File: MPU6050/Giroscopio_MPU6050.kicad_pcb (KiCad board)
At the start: 2 copper layers, 15.1 x 16.7 mm, 7 parts, among them U301 MPU-6050

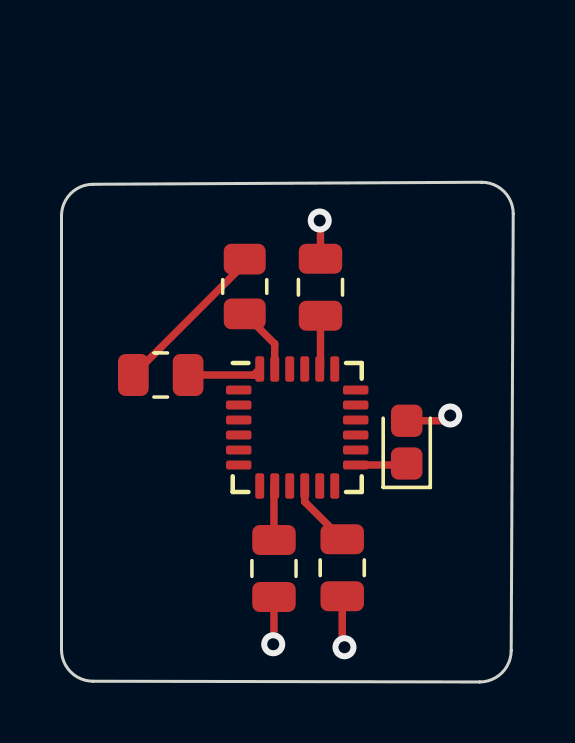
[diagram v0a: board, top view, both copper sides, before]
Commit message: MPU6050: modificato il leggermente il disegno
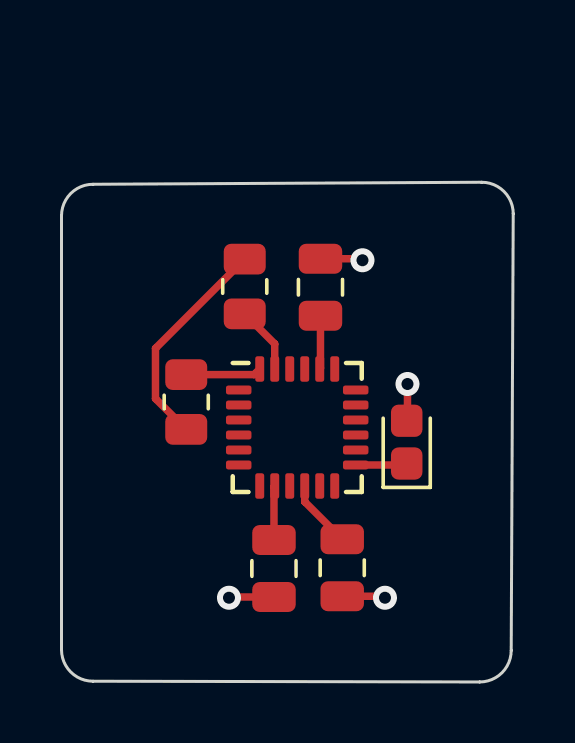
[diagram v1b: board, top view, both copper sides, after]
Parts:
- moved R401 1.24 mm to (158.8, 63.2), turned to 90 degrees
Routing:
- net VCC_3.3v: track 5.40 -> 7.48 mm
- net GND: track 6.12 -> 5.61 mm
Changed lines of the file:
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@@
   )
   (footprint "Resistor_SMD:R_0805_2012Metric" (layer "F.Cu")
-    (at 157.95 62.3)
+    (at 158.8 63.2 90)
     (descr "Resistor SMD 0805 (2012 Metric), square (rectangular) end terminal, IPC_7351 nominal, (Body size source: IPC-SM-782 page 72, https://www.pcb-3d.com/wordpress/wp-content/uploads/ipc-sm-782a_amendment_1_and_2.pdf), generated with kicad-footprint-generator")
     (tags "resistor")
@@
     (property "Sheetname" "")
     (attr smd)
-    (fp_text reference "R401" (at 0 -1.65) (layer "F.Fab")
+    (fp_text reference "R401" (at 0 -1.65 90) (layer "F.Fab")
       (effects (font (size 1 1) (thickness 0.15)))
     )
-    (fp_text value "4.7k" (at 0 1.65) (layer "F.Fab")
+    (fp_text value "4.7k" (at 0 1.65 90) (layer "F.Fab")
       (effects (font (size 1 1) (thickness 0.15)))
     )
-    (fp_text user "${REFERENCE}" (at 0 0) (layer "F.Fab")
+    (fp_text user "${REFERENCE}" (at 0 0 90) (layer "F.Fab")
       (effects (font (size 0.5 0.5) (thickness 0.08)))
     )
@@
     (fp_line (start -1 0.625) (end -1 -0.625) (layer "F.Fab") (width 0.1))
     (fp_line (start 1 -0.625) (end 1 0.625) (layer "F.Fab") (width 0.1))
-    (pad "1" smd roundrect (at -0.9125 0) (size 1.025 1.4) (layers "F.Cu" "F.Paste" "F.Mask") (roundrect_rratio 0.243902)
+    (pad "1" smd roundrect (at -0.9125 0 90) (size 1.025 1.4) (layers "F.Cu" "F.Paste" "F.Mask") (roundrect_rratio 0.243902)
       (net 6 "VCC_3.3v") (pintype "passive"))
-    (pad "2" smd roundrect (at 0.9125 0) (size 1.025 1.4) (layers "F.Cu" "F.Paste" "F.Mask") (roundrect_rratio 0.243902)
+    (pad "2" smd roundrect (at 0.9125 0 90) (size 1.025 1.4) (layers "F.Cu" "F.Paste" "F.Mask") (roundrect_rratio 0.243902)
       (net 7 "Net-(U301-Pad24)") (pintype "passive"))
     (model "${KICAD6_3DMODEL_DIR}/Resistor_SMD.3dshapes/R_0805_2012Metric.wrl"
@@
   (segment (start 166.15 65.25) (end 166.1 65.3) (width 0.25) (layer "F.Cu") (net 1))
   (segment (start 166.1 65.3) (end 164.45 65.3) (width 0.25) (layer "F.Cu") (net 1))
-  (segment (start 166.15 63.825) (end 167.425 63.825) (width 0.25) (layer "F.Cu") (net 2))
-  (segment (start 161.725 71.25) (end 161.7 71.275) (width 0.25) (layer "F.Cu") (net 2))
-  (segment (start 164 71.3) (end 164.075 71.375) (width 0.25) (layer "F.Cu") (net 2))
-  (segment (start 163.275 57.175) (end 163.25 57.15) (width 0.25) (layer "F.Cu") (net 2))
-  (segment (start 167.425 63.825) (end 167.6 63.65) (width 0.25) (layer "F.Cu") (net 2))
-  (segment (start 161.725 69.7) (end 161.725 71.25) (width 0.25) (layer "F.Cu") (net 2))
-  (segment (start 164 69.675) (end 164 71.3) (width 0.25) (layer "F.Cu") (net 2))
-  (segment (start 163.275 58.425) (end 163.275 57.175) (width 0.25) (layer "F.Cu") (net 2))
-  (via (at 164.075 71.375) (size 0.8) (drill 0.4) (layers "F.Cu" "B.Cu") (net 2))
-  (via (at 167.6 63.65) (size 0.8) (drill 0.4) (layers "F.Cu" "B.Cu") (net 2))
-  (via (at 163.25 57.15) (size 0.8) (drill 0.4) (layers "F.Cu" "B.Cu") (net 2))
-  (via (at 161.7 71.275) (size 0.8) (drill 0.4) (layers "F.Cu" "B.Cu") (net 2))
+  (segment (start 160.25 69.7) (end 160.225 69.725) (width 0.25) (layer "F.Cu") (net 2))
+  (segment (start 165.375 69.675) (end 165.425 69.725) (width 0.25) (layer "F.Cu") (net 2))
+  (segment (start 161.725 69.7) (end 160.25 69.7) (width 0.25) (layer "F.Cu") (net 2))
+  (segment (start 166.175 63.8) (end 166.15 63.825) (width 0.25) (layer "F.Cu") (net 2))
+  (segment (start 166.175 62.6) (end 166.175 63.8) (width 0.25) (layer "F.Cu") (net 2))
+  (segment (start 163.275 58.425) (end 164.625 58.425) (width 0.25) (layer "F.Cu") (net 2))
+  (segment (start 164.625 58.425) (end 164.675 58.475) (width 0.25) (layer "F.Cu") (net 2))
+  (segment (start 164 69.675) (end 165.375 69.675) (width 0.25) (layer "F.Cu") (net 2))
+  (via (at 165.425 69.725) (size 0.8) (drill 0.4) (layers "F.Cu" "B.Cu") (net 2))
+  (via (at 166.175 62.6) (size 0.8) (drill 0.4) (layers "F.Cu" "B.Cu") (net 2))
+  (via (at 164.675 58.475) (size 0.8) (drill 0.4) (layers "F.Cu" "B.Cu") (net 2))
+  (via (at 160.225 69.725) (size 0.8) (drill 0.4) (layers "F.Cu" "B.Cu") (net 2))
   (segment (start 162.75 66.525) (end 162.75 66) (width 0.25) (layer "F.Cu") (net 3))
   (segment (start 164 67.775) (end 162.75 66.525) (width 0.25) (layer "F.Cu") (net 3))
@@
   (segment (start 161.725 67.8) (end 161.725 66.025) (width 0.25) (layer "F.Cu") (net 5))
   (segment (start 161.725 66.025) (end 161.75 66) (width 0.25) (layer "F.Cu") (net 5))
-  (segment (start 160.75 58.5875) (end 157.0375 62.3) (width 0.25) (layer "F.Cu") (net 6))
+  (segment (start 157.775 61.4125) (end 160.75 58.4375) (width 0.25) (layer "F.Cu") (net 6))
   (segment (start 160.75 58.4375) (end 160.75 58.5875) (width 0.25) (layer "F.Cu") (net 6))
-  (segment (start 158.8625 62.3) (end 161.05 62.3) (width 0.25) (layer "F.Cu") (net 7))
-  (segment (start 161.05 62.3) (end 161.25 62.1) (width 0.25) (layer "F.Cu") (net 7))
+  (segment (start 158.8 64.1125) (end 157.775 63.0875) (width 0.25) (layer "F.Cu") (net 6))
+  (segment (start 157.775 63.0875) (end 157.775 61.4125) (width 0.25) (layer "F.Cu") (net 6))
+  (segment (start 158.8 62.2875) (end 161.0625 62.2875) (width 0.25) (layer "F.Cu") (net 7))
+  (segment (start 161.0625 62.2875) (end 161.25 62.1) (width 0.25) (layer "F.Cu") (net 7))
   (segment (start 160.75 60.2625) (end 161.75 61.2625) (width 0.25) (layer "F.Cu") (net 8))
   (segment (start 161.75 61.2625) (end 161.75 62.1) (width 0.25) (layer "F.Cu") (net 8))

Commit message: MPU6050: creazione del PCB e layout NON completo
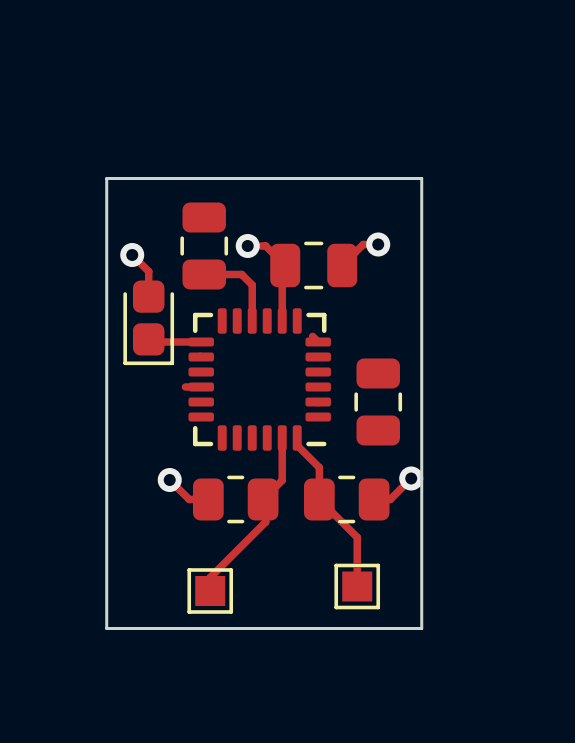
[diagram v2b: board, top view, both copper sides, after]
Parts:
- added J401: Conn_01x01_Female, TestPoint:TestPoint_Pad_1.0x1.0mm, F.Cu at (164.5, 69.3)
- added J402: Conn_01x01_Female, TestPoint:TestPoint_Pad_1.0x1.0mm, F.Cu at (159.6, 69.5)
- moved C402 11.7 mm to (159.4, 58.0), turned to 90 degrees
- moved C404 10.2 mm to (163.1, 58.6), turned to 180 degrees
- moved C401 9.54 mm to (157.6, 60.4)
- moved R402 7.11 mm to (160.4, 66.5), turned to 0 degrees
- moved R401 6.26 mm to (164.2, 66.5), turned to 0 degrees
- moved C403 4.28 mm to (165.2, 63.2), turned to -90 degrees
- moved U301 2.03 mm to (161.2, 62.5), turned to 180 degrees
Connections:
- net Net-(U301-Pad23) renamed GYRO_SCL
- C403 pad 1: Net-(C403-Pad1) -> GND
- C403 pad 2: GND -> GYRO_CPOUT
- R401 pad 1: VCC_3.3v -> GYRO_SDA
- R401 pad 2: Net-(U301-Pad24) -> VCC_3.3v
- U301 pad 20: Net-(C403-Pad1) -> GYRO_CPOUT
- U301 pad 24: Net-(U301-Pad24) -> GYRO_SDA
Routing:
- net GYRO_SDA: track 0.00 -> 5.88 mm
- net VCC_3.3v: track 7.48 -> 3.08 mm, vias 0 -> 2
- net GYRO_SCL: track 2.25 -> 6.17 mm
- net Net-(U301-Pad24): track 2.53 -> 0.00 mm
- net GND: track 5.61 -> 3.11 mm, vias 4 -> 2
- net Net-(C403-Pad1): track 1.79 -> 0.00 mm
- net VCC3.3: track 1.81 -> 3.41 mm, vias 0 -> 1
- net Net-(C402-Pad1): track 2.29 -> 2.94 mm
- net unconnected-(U301-Pad16): track 0.00 -> 0.53 mm
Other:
- board size 15.1 x 16.7 mm -> 10.5 x 15 mm

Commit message: mpu6050: aggiunta testpad
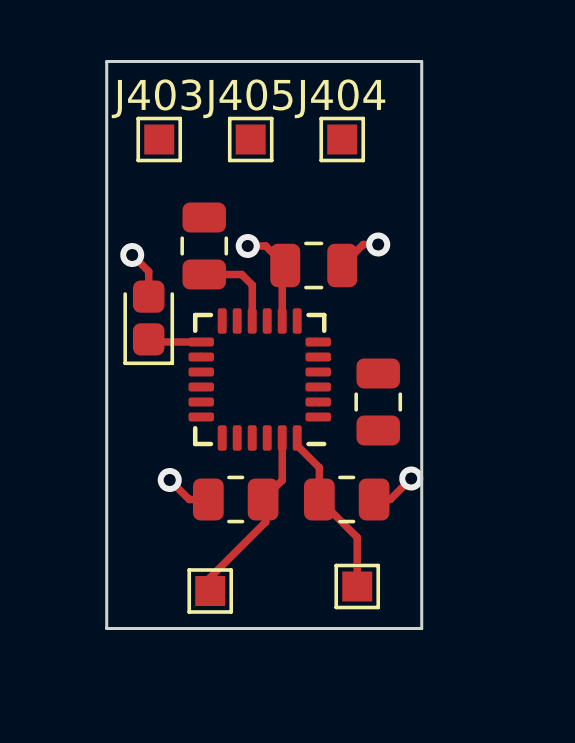
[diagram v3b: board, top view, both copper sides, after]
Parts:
- added J403: Conn_01x01_Female, TestPoint:TestPoint_Pad_1.0x1.0mm, F.Cu at (157.9, 54.5)
- added J404: Conn_01x01_Female, TestPoint:TestPoint_Pad_1.0x1.0mm, F.Cu at (164.0, 54.5)
- added J405: Conn_01x01_Female, TestPoint:TestPoint_Pad_1.0x1.0mm, F.Cu at (160.9, 54.5)
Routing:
- net unconnected-(U301-Pad16): track 0.53 -> 0.00 mm
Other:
- board size 10.5 x 15 mm -> 10.5 x 18.9 mm
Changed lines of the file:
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@@
     )
+  )
+  (footprint "TestPoint:TestPoint_Pad_1.0x1.0mm" (layer "F.Cu")
+    (at 160.95 54.45)
+    (descr "SMD rectangular pad as test Point, square 1.0mm side length")
+    (tags "test point SMD pad rectangle square")
+    (property "Sheetfile" "Giroscopio_MPU6050.kicad_sch")
+    (property "Sheetname" "")
+    (attr exclude_from_pos_files)
+    (fp_text reference "J405" (at 0 -1.448) (layer "F.SilkS")
+      (effects (font (size 1 1) (thickness 0.15)))
+    )
+    (fp_text value "Conn_01x01_Female" (at 0 1.55) (layer "F.Fab")
+      (effects (font (size 1 1) (thickness 0.15)))
+    )
+    (fp_text user "${REFERENCE}" (at 0 -1.45) (layer "F.Fab")
+      (effects (font (size 1 1) (thickness 0.15)))
+    )
+    (fp_line (start 0.7 -0.7) (end 0.7 0.7) (layer "F.SilkS") (width 0.12))
+    (fp_line (start -0.7 -0.7) (end 0.7 -0.7) (layer "F.SilkS") (width 0.12))
+    (fp_line (start 0.7 0.7) (end -0.7 0.7) (layer "F.SilkS") (width 0.12))
+    (fp_line (start -0.7 0.7) (end -0.7 -0.7) (layer "F.SilkS") (width 0.12))
+    (fp_line (start 1 1) (end -1 1) (layer "F.CrtYd") (width 0.05))
+    (fp_line (start 1 1) (end 1 -1) (layer "F.CrtYd") (width 0.05))
+    (fp_line (start -1 -1) (end 1 -1) (layer "F.CrtYd") (width 0.05))
+    (fp_line (start -1 -1) (end -1 1) (layer "F.CrtYd") (width 0.05))
+    (pad "1" smd rect (at 0 0) (size 1 1) (layers "F.Cu" "F.Mask")
+      (net 5 "VCC3.3") (pinfunction "Pin_1") (pintype "passive"))
   )
   (footprint "Resistor_SMD:R_0805_2012Metric" (layer "F.Cu")
@@
     )
   )
+  (footprint "TestPoint:TestPoint_Pad_1.0x1.0mm" (layer "F.Cu")
+    (at 157.9 54.45)
+    (descr "SMD rectangular pad as test Point, square 1.0mm side length")
+    (tags "test point SMD pad rectangle square")
+    (property "Sheetfile" "Giroscopio_MPU6050.kicad_sch")
+    (property "Sheetname" "")
+    (attr exclude_from_pos_files)
+    (fp_text reference "J403" (at 0 -1.448) (layer "F.SilkS")
+      (effects (font (size 1 1) (thickness 0.15)))
+    )
+    (fp_text value "Conn_01x01_Female" (at 0 1.55) (layer "F.Fab")
+      (effects (font (size 1 1) (thickness 0.15)))
+    )
+    (fp_text user "${REFERENCE}" (at 0 -1.45) (layer "F.Fab")
+      (effects (font (size 1 1) (thickness 0.15)))
+    )
+    (fp_line (start 0.7 -0.7) (end 0.7 0.7) (layer "F.SilkS") (width 0.12))
+    (fp_line (start 0.7 0.7) (end -0.7 0.7) (layer "F.SilkS") (width 0.12))
+    (fp_line (start -0.7 0.7) (end -0.7 -0.7) (layer "F.SilkS") (width 0.12))
+    (fp_line (start -0.7 -0.7) (end 0.7 -0.7) (layer "F.SilkS") (width 0.12))
+    (fp_line (start 1 1) (end 1 -1) (layer "F.CrtYd") (width 0.05))
+    (fp_line (start -1 -1) (end -1 1) (layer "F.CrtYd") (width 0.05))
+    (fp_line (start -1 -1) (end 1 -1) (layer "F.CrtYd") (width 0.05))
+    (fp_line (start 1 1) (end -1 1) (layer "F.CrtYd") (width 0.05))
+    (pad "1" smd rect (at 0 0) (size 1 1) (layers "F.Cu" "F.Mask")
+      (net 14 "GYRO_INT") (pinfunction "Pin_1") (pintype "passive"))
+  )
   (footprint "Resistor_SMD:R_0805_2012Metric" (layer "F.Cu")
     (at 164.15 66.45)
@@
     )
   )
+  (footprint "TestPoint:TestPoint_Pad_1.0x1.0mm" (layer "F.Cu")
+    (at 164 54.45)
+    (descr "SMD rectangular pad as test Point, square 1.0mm side length")
+    (tags "test point SMD pad rectangle square")
+    (property "Sheetfile" "Giroscopio_MPU6050.kicad_sch")
+    (property "Sheetname" "")
+    (attr exclude_from_pos_files)
+    (fp_text reference "J404" (at 0 -1.448) (layer "F.SilkS")
+      (effects (font (size 1 1) (thickness 0.15)))
+    )
+    (fp_text value "Conn_01x01_Female" (at 0 1.55) (layer "F.Fab")
+      (effects (font (size 1 1) (thickness 0.15)))
+    )
+    (fp_text user "${REFERENCE}" (at 0 -1.45) (layer "F.Fab")
+      (effects (font (size 1 1) (thickness 0.15)))
+    )
+    (fp_line (start -0.7 0.7) (end -0.7 -0.7) (layer "F.SilkS") (width 0.12))
+    (fp_line (start -0.7 -0.7) (end 0.7 -0.7) (layer "F.SilkS") (width 0.12))
+    (fp_line (start 0.7 0.7) (end -0.7 0.7) (layer "F.SilkS") (width 0.12))
+    (fp_line (start 0.7 -0.7) (end 0.7 0.7) (layer "F.SilkS") (width 0.12))
+    (fp_line (start 1 1) (end 1 -1) (layer "F.CrtYd") (width 0.05))
+    (fp_line (start -1 -1) (end 1 -1) (layer "F.CrtYd") (width 0.05))
+    (fp_line (start 1 1) (end -1 1) (layer "F.CrtYd") (width 0.05))
+    (fp_line (start -1 -1) (end -1 1) (layer "F.CrtYd") (width 0.05))
+    (pad "1" smd rect (at 0 0) (size 1 1) (layers "F.Cu" "F.Mask")
+      (net 2 "GND") (pinfunction "Pin_1") (pintype "passive"))
+  )
   (footprint "Capacitor_SMD:C_0805_2012Metric" (layer "F.Cu")
     (at 159.4 58 90)
@@
     )
   )
-  (gr_rect (start 156.15 70.75) (end 166.65 55.75) (layer "Edge.Cuts") (width 0.1) (fill none))
+  (gr_rect (start 156.15 70.75) (end 166.65 51.85) (layer "Edge.Cuts") (width 0.1) (fill none))
   (segment (start 159.3 61.2) (end 157.6375 61.2) (width 0.25) (layer "F.Cu") (net 1))
   (segment (start 157.6375 61.2) (end 157.55 61.1125) (width 0.25) (layer "F.Cu") (net 1))
@@
   (via (at 158.25 65.8) (size 0.8) (drill 0.4) (layers "F.Cu" "B.Cu") (net 6))
   (segment (start 163.225 63.225) (end 163.2 63.2) (width 0.25) (layer "F.Cu") (net 7))
-  (segment (start 163.0125 61.0125) (end 163.2 61.2) (width 0.25) (layer "F.Cu") (net 11))
   (segment (start 159.275 61.675) (end 159.3 61.7) (width 0.25) (layer "F.Cu") (net 15))
-  (segment (start 158.775 62.7) (end 159.3 62.7) (width 0.25) (layer "F.Cu") (net 17))
   (segment (start 162.5 64.65) (end 163.2375 65.3875) (width 0.25) (layer "F.Cu") (net 22))
   (segment (start 163.2375 66.45) (end 164.5 67.7125) (width 0.25) (layer "F.Cu") (net 22))
